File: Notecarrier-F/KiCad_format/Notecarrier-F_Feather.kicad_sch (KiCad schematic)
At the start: 13 parts, among them J7 SM04B-SRSS-TB(LF)(SN), J8 SM04B-SRSS-TB(LF)(SN), SW3 PTS810-SJS-250-SMTR-LFS, SW4 CJS-1200TA, SW5 CJS-1200TA, U4 TXS0102DCU, U6 DGQ2788AEN-T1-GE4

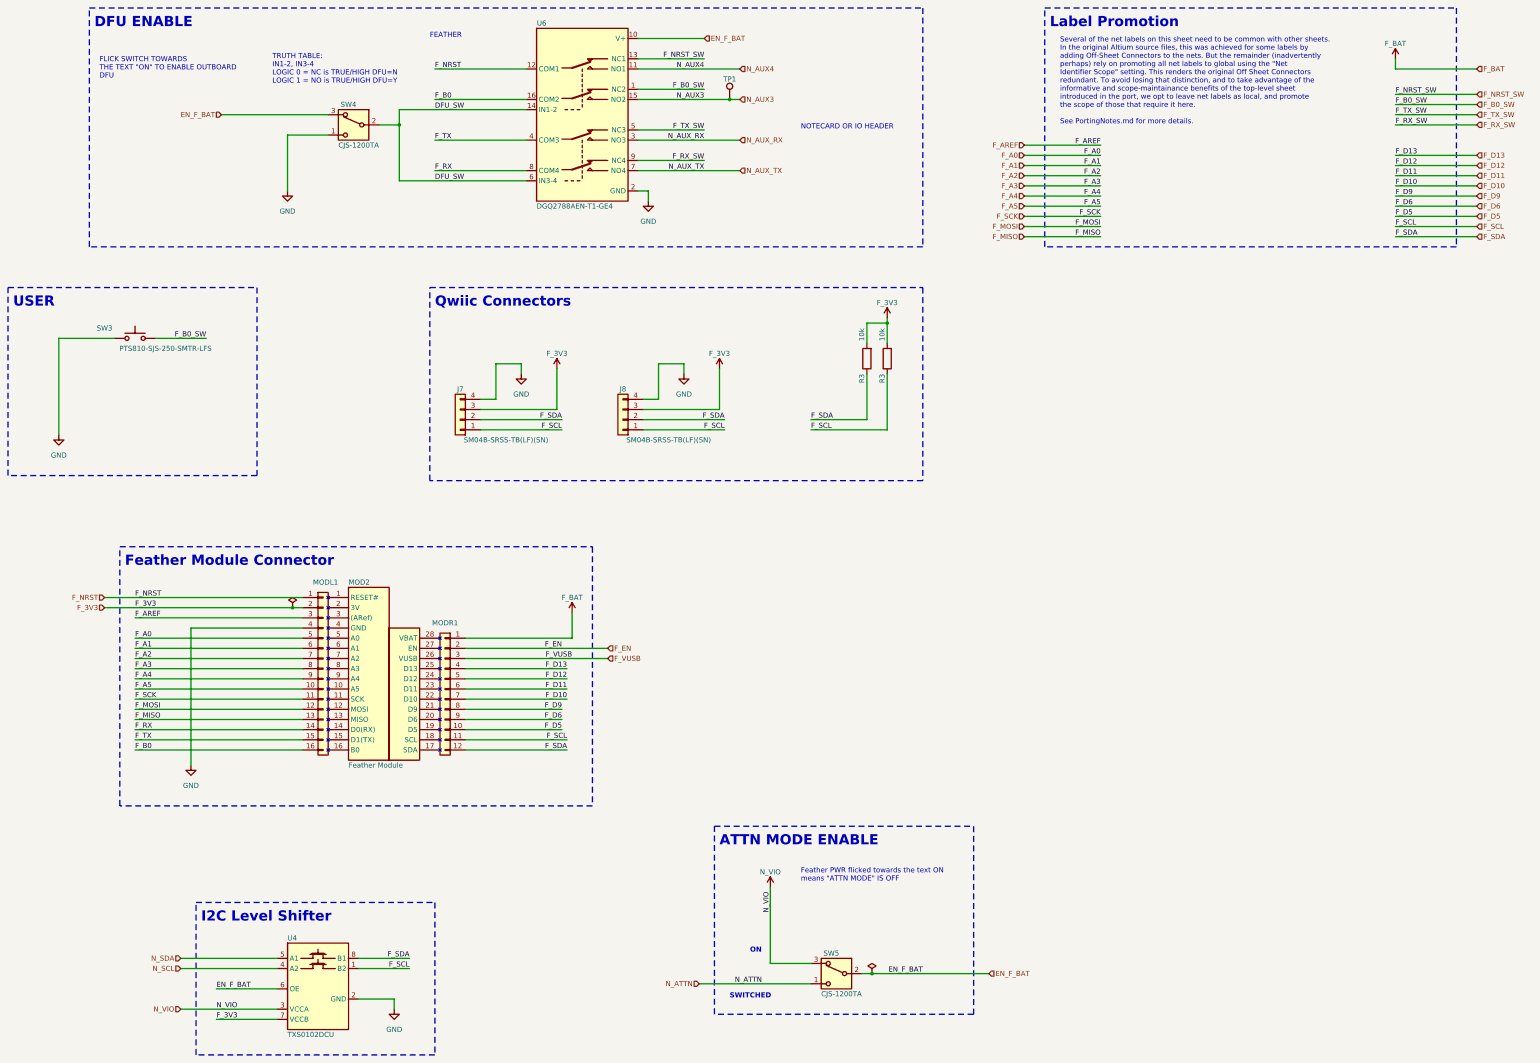
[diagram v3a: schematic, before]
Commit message: Apply first pass validation of Notecarrier-F port
Huge push to identify, solve, document and revalidate all the details revealed by the first run of the validation process. Validation is now acceptable and preparation can be made to release Rev A.
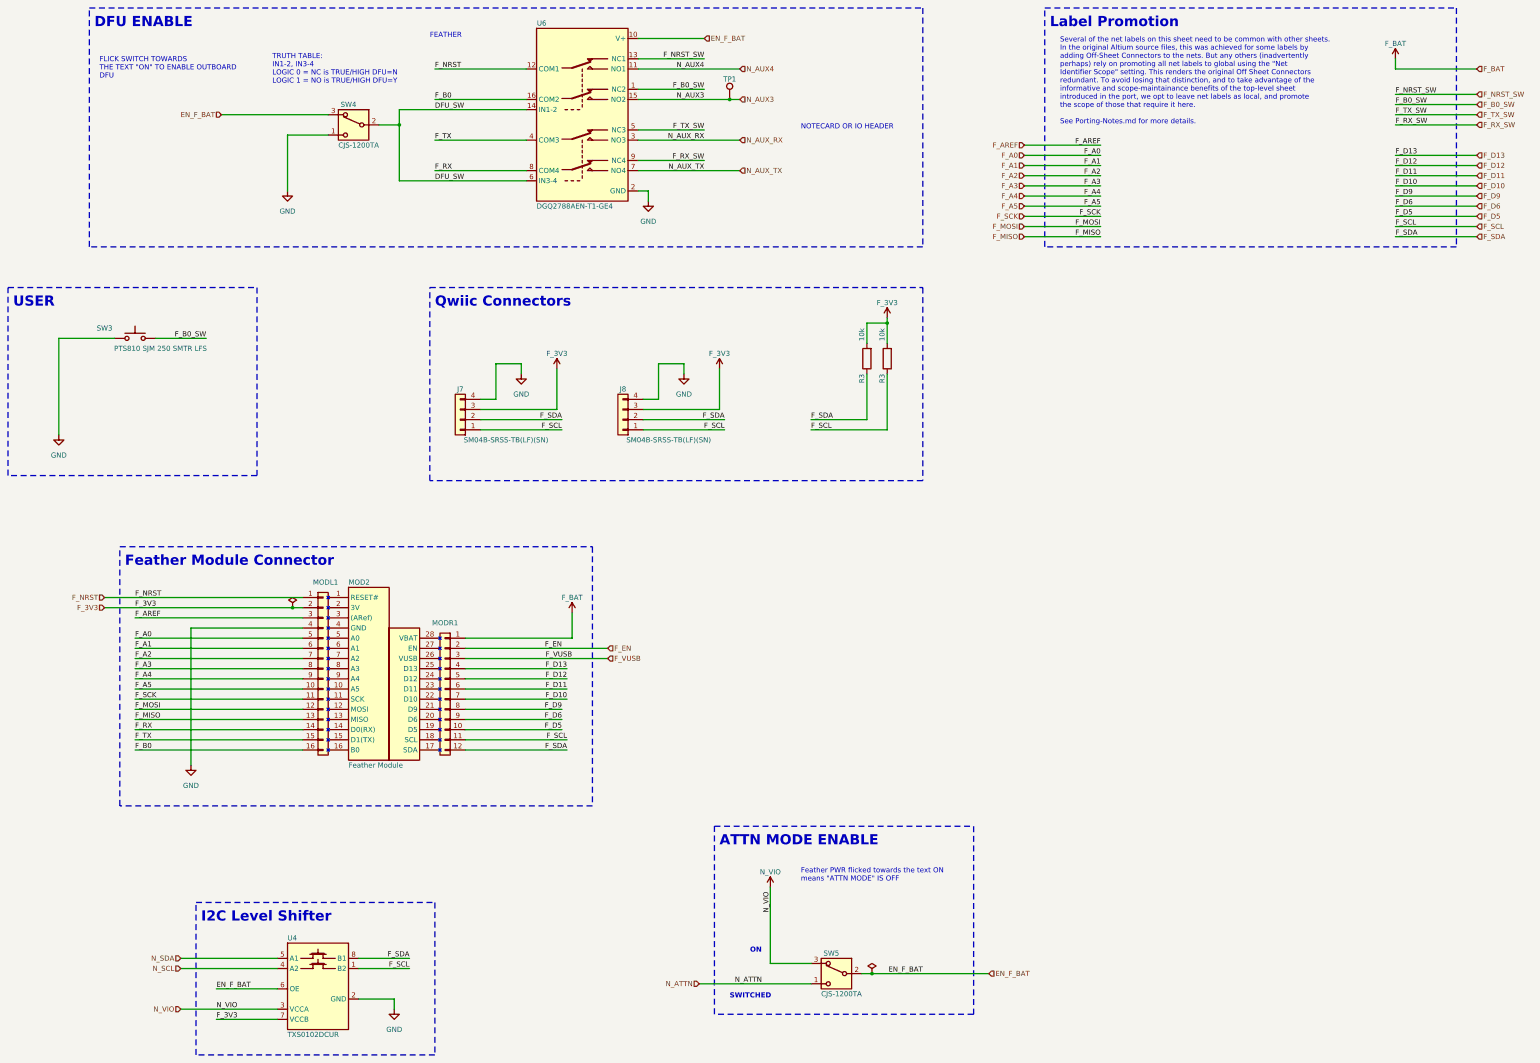
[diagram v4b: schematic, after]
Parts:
- SW3: value PTS810-SJS-250-SMTR-LFS -> PTS810 SJM 250 SMTR LFS; symbol blues-kicad-lib:PTS810-SJS-250-SMTR-LFS -> blues-kicad-lib:PTS810-SJM-250-SMTR-LFS
- U4: value TXS0102DCU -> TXS0102DCUR
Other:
- note added: "Several of the net labels on this sheet need to be common with other sheets. In the original Altium source files, this was achieved for some labels by adding Off-Sheet Connectors to the nets. But any others (inadvertently perhaps) rely on promoting all net labels to global using the "Net Identifier Scope" setting. This renders the original Off Sheet Connectors redundant. To avoid losing that dist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"
- note removed: "Several of the net labels on this sheet need to be common with other sheets. In the original Altium source files, this was achieved for some labels by adding Off-Sheet Connectors to the nets. But the remainder (inadvertently perhaps) rely on promoting all net labels to global using the "Net Identifier Scope" setting. This renders the original Off Sheet Connectors redundant. To avoid losing that d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"
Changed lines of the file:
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@@
     (effects (font (size 2.54 2.54) (thickness 0.508) bold) (justify left bottom))
   )
-  (text "Several of the net labels on this sheet need to be common with other sheets.\nIn the original Altium source files, this was achieved for some labels by\nadding Off-Sheet Connectors to the nets. But the remainder (inadvertently\nperhaps) rely on promoting all net labels to global using the \"Net\nIdentifier Scope\" setting. This renders the original Off Sheet Connectors\nredundant. To avoid losing that distinction, and to take advantage of the\ninformative and scope-maintainance benefits of the top-level sheet\nintroduced in the port, we opt to leave net labels as local, and promote\nthe scope of those that require it here.\n\nSee PortingNotes.md for more details."
+  (text "Several of the net labels on this sheet need to be common with other sheets.\nIn the original Altium source files, this was achieved for some labels by\nadding Off-Sheet Connectors to the nets. But any others (inadvertently\nperhaps) rely on promoting all net labels to global using the \"Net\nIdentifier Scope\" setting. This renders the original Off Sheet Connectors\nredundant. To avoid losing that distinction, and to take advantage of the\ninformative and scope-maintainance benefits of the top-level sheet\nintroduced in the port, we opt to leave net labels as local, and promote\nthe scope of those that require it here.\n\nSee Porting-Notes.md for more details."
     (at 284.48 46.99 0)
     (effects (font (size 1.27 1.27)) (justify left bottom))
@@
     )
   )
-  (symbol (lib_id "blues-kicad-lib:PTS810-SJS-250-SMTR-LFS") (at 53.34 100.33 0) (unit 1)
+  (symbol (lib_id "blues-kicad-lib:PTS810-SJM-250-SMTR-LFS") (at 53.34 100.33 0) (unit 1)
     (in_bom yes) (on_board yes) (dnp no)
     (property "Reference" "SW3" (at 45.72 97.79 0)
       (effects (font (size 1.27 1.27)))
     )
-    (property "Value" "PTS810-SJS-250-SMTR-LFS" (at 60.96 102.87 0)
+    (property "Value" "PTS810 SJM 250 SMTR LFS" (at 59.69 102.87 0)
       (effects (font (size 1.27 1.27)))
     )
@@
       (effects (font (size 1.27 1.27)) (justify left))
     )
-    (property "Value" "TXS0102DCU" (at 91.44 274.32 0)
+    (property "Value" "TXS0102DCUR" (at 91.44 274.32 0)
       (effects (font (size 1.27 1.27)) (justify left))
     )
@@
       (effects (font (size 1.27 1.27)) hide)
     )
+    (property "Critical" "" (at 99.06 262.89 0)
+      (effects (font (size 1.27 1.27)) hide)
+    )

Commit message: Merge pending library into main.
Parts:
- J7, J8: footprint blues-kicad-lib-pending:JST SM04B-SRSS-TB -> blues-kicad-lib:JST SM04B-SRSS-TB
- MOD2: footprint blues-kicad-lib-pending:BLUES_WIRELESS_SWAN_2-54_HEADERS -> blues-kicad-lib:BLUES_WIRELESS_SWAN_2-54_HEADERS
- MODL1: footprint blues-kicad-lib-pending:16PIN_254MM -> blues-kicad-lib:16PIN_254MM
- MODR1: footprint blues-kicad-lib-pending:12PIN_254MM -> blues-kicad-lib:12PIN_254MM
- R3: footprint blues-kicad-lib-pending:RES 0402_1005 -> blues-kicad-lib:RES 0402_1005
- SW3: footprint blues-kicad-lib-pending:C&K PTS810 -> blues-kicad-lib:C&K PTS810
- SW4, SW5: footprint blues-kicad-lib-pending:SW_CJS-1200TA -> blues-kicad-lib:SW_CJS-1200TA
- TP1: footprint blues-kicad-lib-pending:TESTPAD_127 -> blues-kicad-lib:TESTPAD_127
- U4: footprint blues-kicad-lib-pending:SOP50P310X90-8N -> blues-kicad-lib:SOP50P310X90-8N
- U6: footprint blues-kicad-lib-pending:QFN40P260X180X60-16N -> blues-kicad-lib:QFN40P260X180X60-16N
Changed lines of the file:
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@@
       (effects (font (size 1.27 1.27)))
     )
-    (property "Footprint" "blues-kicad-lib-pending:JST SM04B-SRSS-TB" (at 134.62 120.65 0)
+    (property "Footprint" "blues-kicad-lib:JST SM04B-SRSS-TB" (at 134.62 120.65 0)
       (effects (font (size 1.27 1.27)) hide)
     )
@@
       (effects (font (size 1.27 1.27)) (justify right))
     )
-    (property "Footprint" "blues-kicad-lib-pending:SW_CJS-1200TA" (at 106.68 54.61 0)
+    (property "Footprint" "blues-kicad-lib:SW_CJS-1200TA" (at 106.68 54.61 0)
       (effects (font (size 1.27 1.27)) hide)
     )
@@
       (effects (font (size 1.27 1.27)))
     )
-    (property "Footprint" "blues-kicad-lib-pending:C&K PTS810" (at 53.34 95.25 0)
+    (property "Footprint" "blues-kicad-lib:C&K PTS810" (at 53.34 95.25 0)
       (effects (font (size 1.27 1.27)) hide)
     )
@@
       (effects (font (size 1.27 1.27)) (justify right))
     )
-    (property "Footprint" "blues-kicad-lib-pending:SW_CJS-1200TA" (at 227.33 266.7 0)
+    (property "Footprint" "blues-kicad-lib:SW_CJS-1200TA" (at 227.33 266.7 0)
       (effects (font (size 1.27 1.27)) hide)
     )
@@
       (effects (font (size 1.27 1.27)) (justify left))
     )
-    (property "Footprint" "blues-kicad-lib-pending:QFN40P260X180X60-16N" (at 165.1 36.195 90)
+    (property "Footprint" "blues-kicad-lib:QFN40P260X180X60-16N" (at 165.1 36.195 90)
       (effects (font (size 1.27 1.27)) hide)
     )
@@
       (effects (font (size 1.27 1.27)) hide)
     )
-    (property "Footprint" "blues-kicad-lib-pending:12PIN_254MM" (at 130.81 187.96 0)
+    (property "Footprint" "blues-kicad-lib:12PIN_254MM" (at 130.81 187.96 0)
       (effects (font (size 1.27 1.27)) hide)
     )
@@
       (effects (font (size 1.27 1.27)) (justify left))
     )
-    (property "Footprint" "blues-kicad-lib-pending:BLUES_WIRELESS_SWAN_2-54_HEADERS" (at 116.84 194.31 0)
+    (property "Footprint" "blues-kicad-lib:BLUES_WIRELESS_SWAN_2-54_HEADERS" (at 116.84 194.31 0)
       (effects (font (size 1.27 1.27)) hide)
     )
@@
       (effects (font (size 1.27 1.27)) (justify left) hide)
     )
-    (property "Footprint" "blues-kicad-lib-pending:16PIN_254MM" (at 100.33 182.88 0)
+    (property "Footprint" "blues-kicad-lib:16PIN_254MM" (at 100.33 182.88 0)
       (effects (font (size 1.27 1.27)) hide)
     )
@@
       (effects (font (size 1.27 1.27)) (justify left))
     )
-    (property "Footprint" "blues-kicad-lib-pending:RES 0402_1005" (at 243.078 105.41 90)
+    (property "Footprint" "blues-kicad-lib:RES 0402_1005" (at 243.078 105.41 90)
       (effects (font (size 1.27 1.27)) hide)
     )
@@
       (effects (font (size 1.27 1.27)) (justify left) hide)
     )
-    (property "Footprint" "blues-kicad-lib-pending:TESTPAD_127" (at 207.01 40.64 0)
+    (property "Footprint" "blues-kicad-lib:TESTPAD_127" (at 207.01 40.64 0)
       (effects (font (size 1.27 1.27)) hide)
     )
@@
       (effects (font (size 1.27 1.27)) (justify left))
     )
-    (property "Footprint" "blues-kicad-lib-pending:SOP50P310X90-8N" (at 99.06 276.86 0)
+    (property "Footprint" "blues-kicad-lib:SOP50P310X90-8N" (at 99.06 276.86 0)
       (effects (font (size 1.27 1.27)) hide)
     )
@@
       (effects (font (size 1.27 1.27)) (justify left))
     )
-    (property "Footprint" "blues-kicad-lib-pending:RES 0402_1005" (at 237.998 105.41 90)
+    (property "Footprint" "blues-kicad-lib:RES 0402_1005" (at 237.998 105.41 90)
       (effects (font (size 1.27 1.27)) hide)
     )
@@
       (effects (font (size 1.27 1.27)))
     )
-    (property "Footprint" "blues-kicad-lib-pending:JST SM04B-SRSS-TB" (at 175.26 120.65 0)
-      (effects (font (size 1.27 1.27)) hide)
-    )
+    (property "Footprint" "blues-kicad-lib:JST SM04B-SRSS-TB" (at 175.26 120.65 0)
+      (effects (font (size 1.27 1.27)) hide)
+    )
